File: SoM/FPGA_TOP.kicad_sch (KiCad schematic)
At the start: 44 parts, among them U1 CCGM1A1, X1 ECS-5032MV

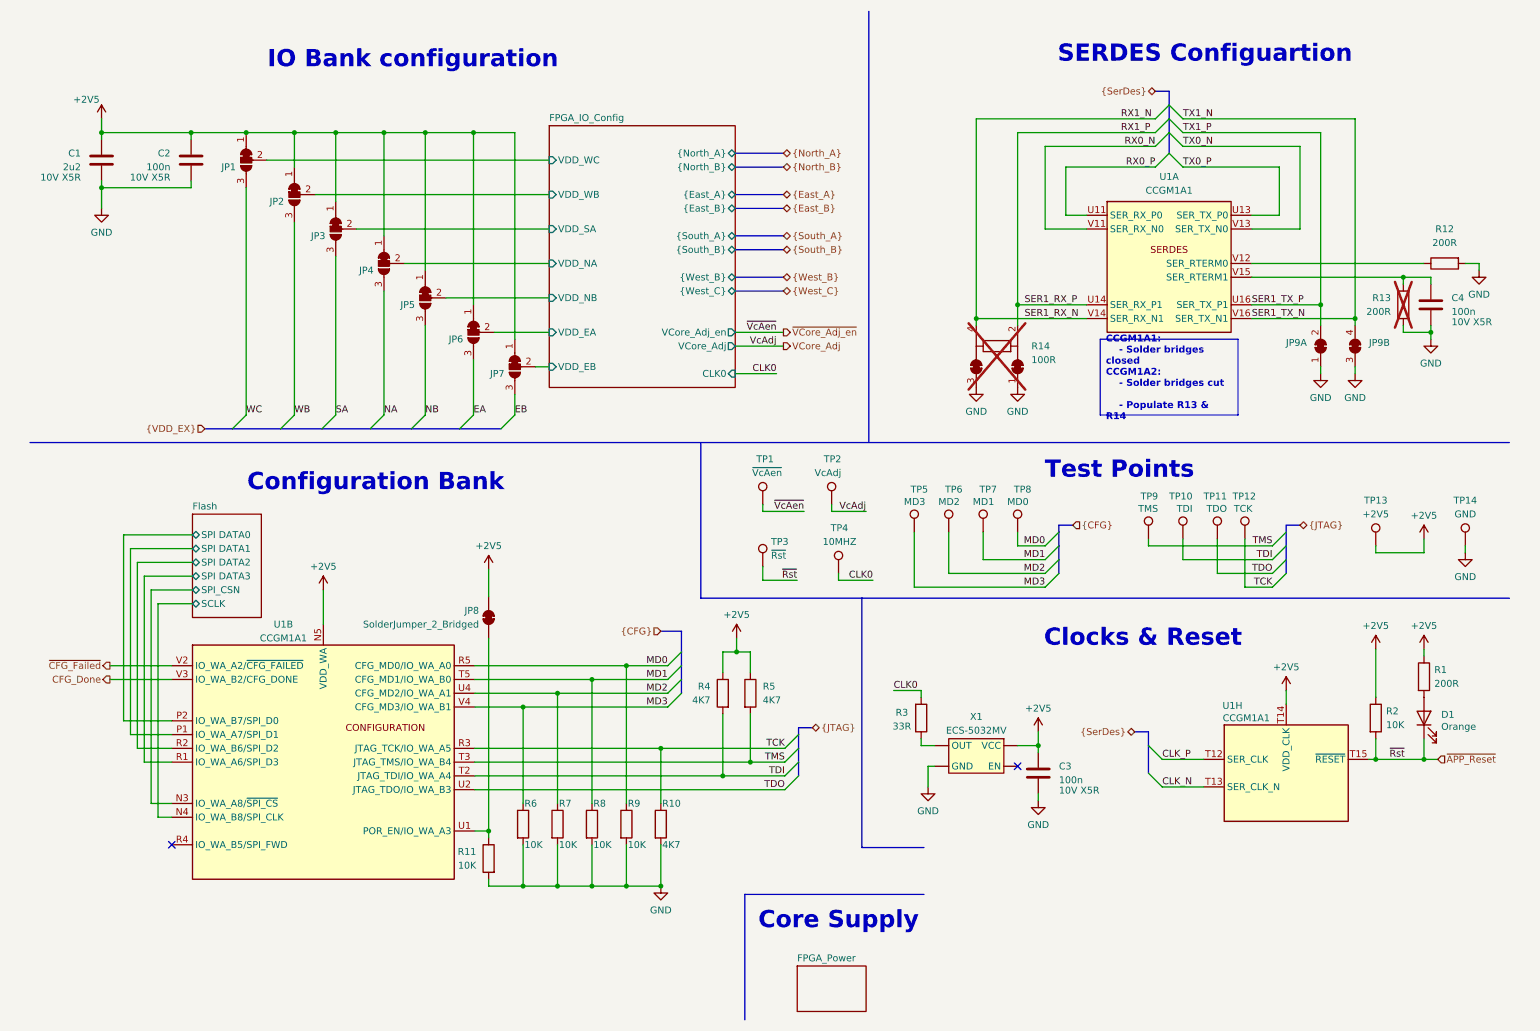
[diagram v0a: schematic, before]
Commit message: Created Version with 0402 components
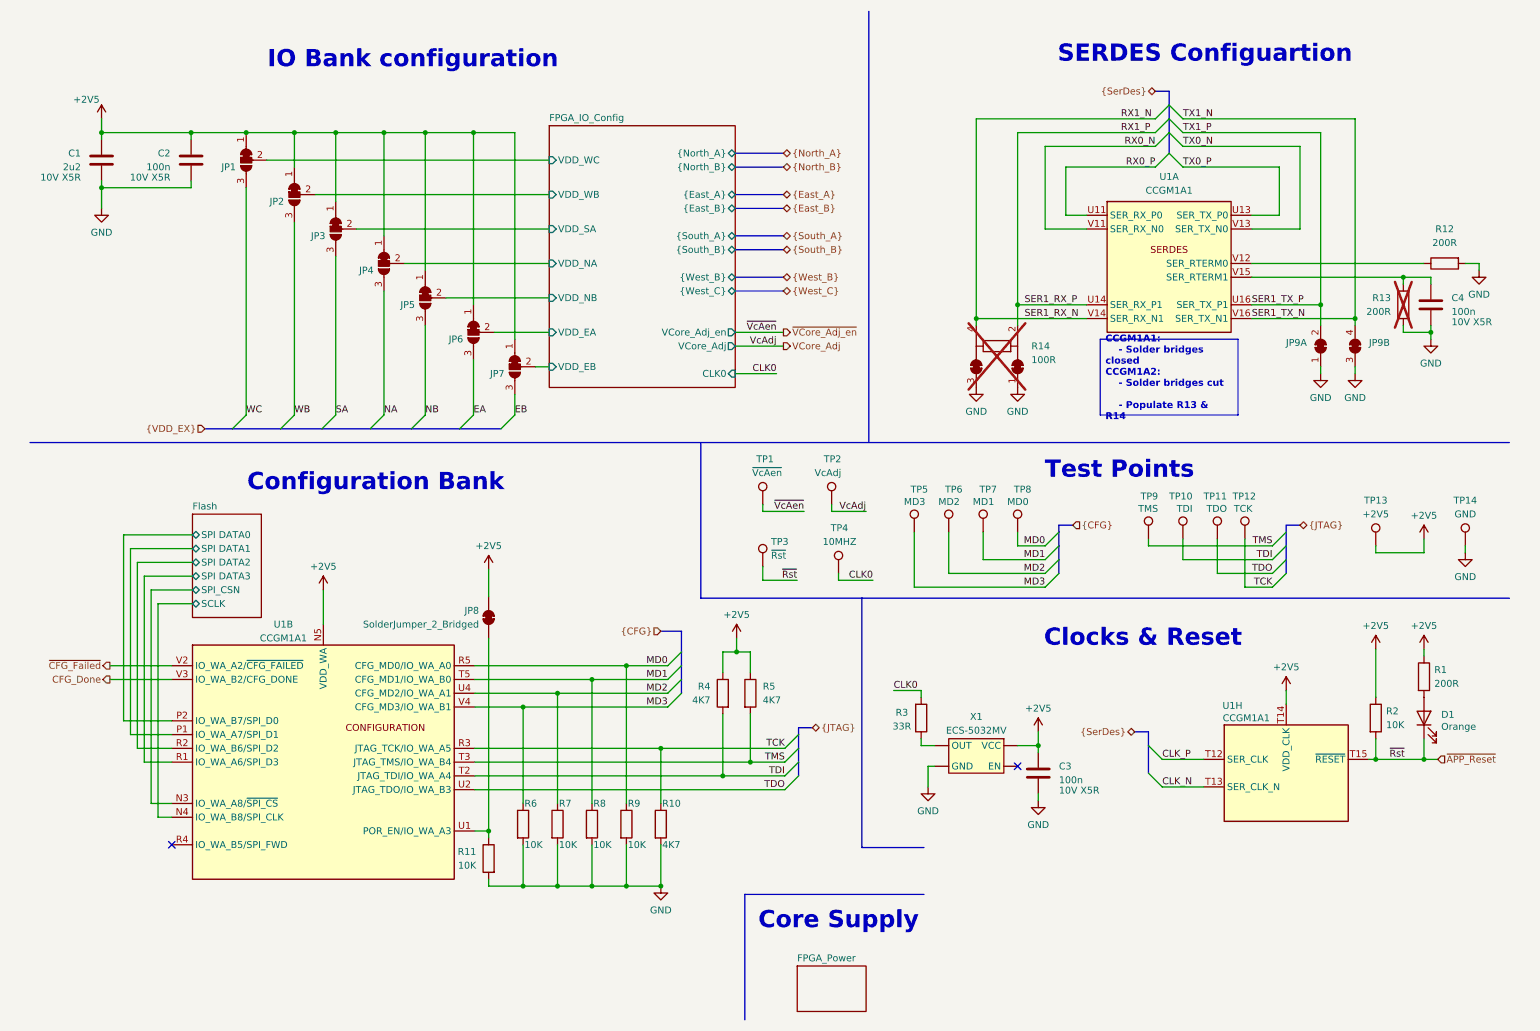
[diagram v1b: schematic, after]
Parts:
- C1: footprint Capacitor_SMD:C_0201_0603Metric -> Capacitor_SMD:C_0402_1005Metric; Mouser Part Number 187-CL03A225KP3CRNC -> GRM155Z71A225KE44D; Part Number (none) -> GRM155Z71A225KE44D
- C2, C3, C4: footprint Capacitor_SMD:C_0201_0603Metric -> Capacitor_SMD:C_0402_1005Metric; Mouser Part Number 187-CL03A104KP3NNNC -> GRM155R71C104KA88J; Part Number (none) -> GRM155R71C104KA88J
- D1: Mouser Part Number 604-APT1608SECK-AMT -> APT1608SECK-AMT; Part Number (none) -> APT1608SECK-AMT
- R1, R12: footprint Resistor_SMD:R_0201_0603Metric -> Resistor_SMD:R_0402_1005Metric; Mouser Part Number 71-CRCW0201-200 -> MCS04020C2000FE000; Part Number (none) -> MCS04020C2000FE000
- R10, R4, R5: footprint Resistor_SMD:R_0201_0603Metric -> Resistor_SMD:R_0402_1005Metric; Mouser Part Number 71-CRCW0201-10K -> CRCW04024K70FKED; Part Number (none) -> CRCW04024K70FKED
- R11, R2, R6, R7, R8, R9: footprint Resistor_SMD:R_0201_0603Metric -> Resistor_SMD:R_0402_1005Metric; Mouser Part Number 71-CRCW0201-10K -> MCS0402MC1002FE000; Part Number (none) -> MCS0402MC1002FE000
- R13: footprint Resistor_SMD:R_0201_0603Metric -> Resistor_SMD:R_0402_1005Metric
- R3: footprint Resistor_SMD:R_0201_0603Metric -> Resistor_SMD:R_0402_1005Metric; Mouser Part Number 71-CRCW020133R0FNED -> MCS04020C3309FE000; Part Number (none) -> MCS04020C3309FE000
- U1: Mouser Part Number (none) -> CCGM1A1-BGA324; Part Number (none) -> CCGM1A1-BGA324
- X1: Mouser Part Number 520-5032MV-100-BNT -> ECS-5032MV-100-BN-TR; Part Number (none) -> ECS-5032MV-100-BN-TR
